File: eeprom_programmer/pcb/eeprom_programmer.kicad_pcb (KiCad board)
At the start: 2 copper layers, 60 x 60 mm, 16 parts, among them M1 MountingHole_3.2mm_M3_Pad, M2 MountingHole_3.2mm_M3_Pad, M3 MountingHole_3.2mm_M3_Pad, M4 MountingHole_3.2mm_M3_Pad, SW1 SW_DIP_x03, U1 74HC595, U2 74HC595, U3 74HC595, U4 SST39SF040, U5 AT28C64B

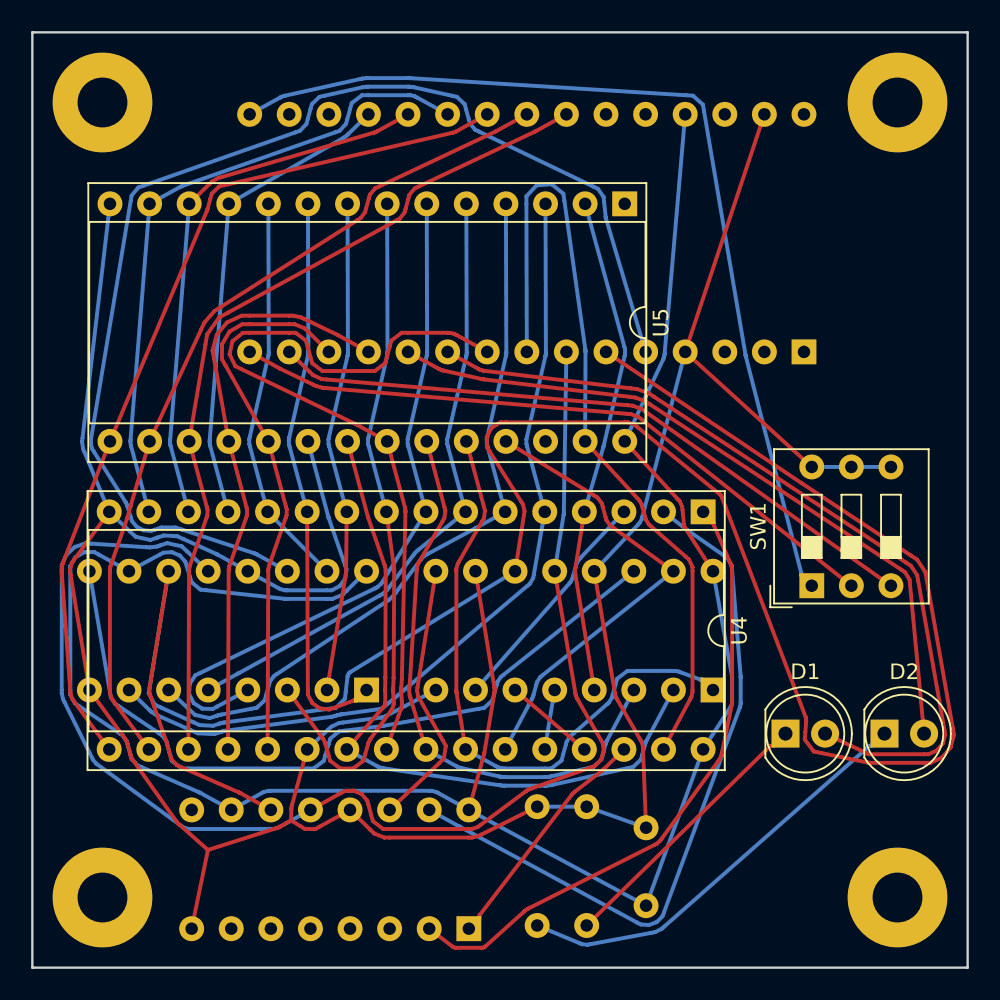
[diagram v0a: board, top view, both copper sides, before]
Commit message: Fix arduino d13 LED pullup bug.
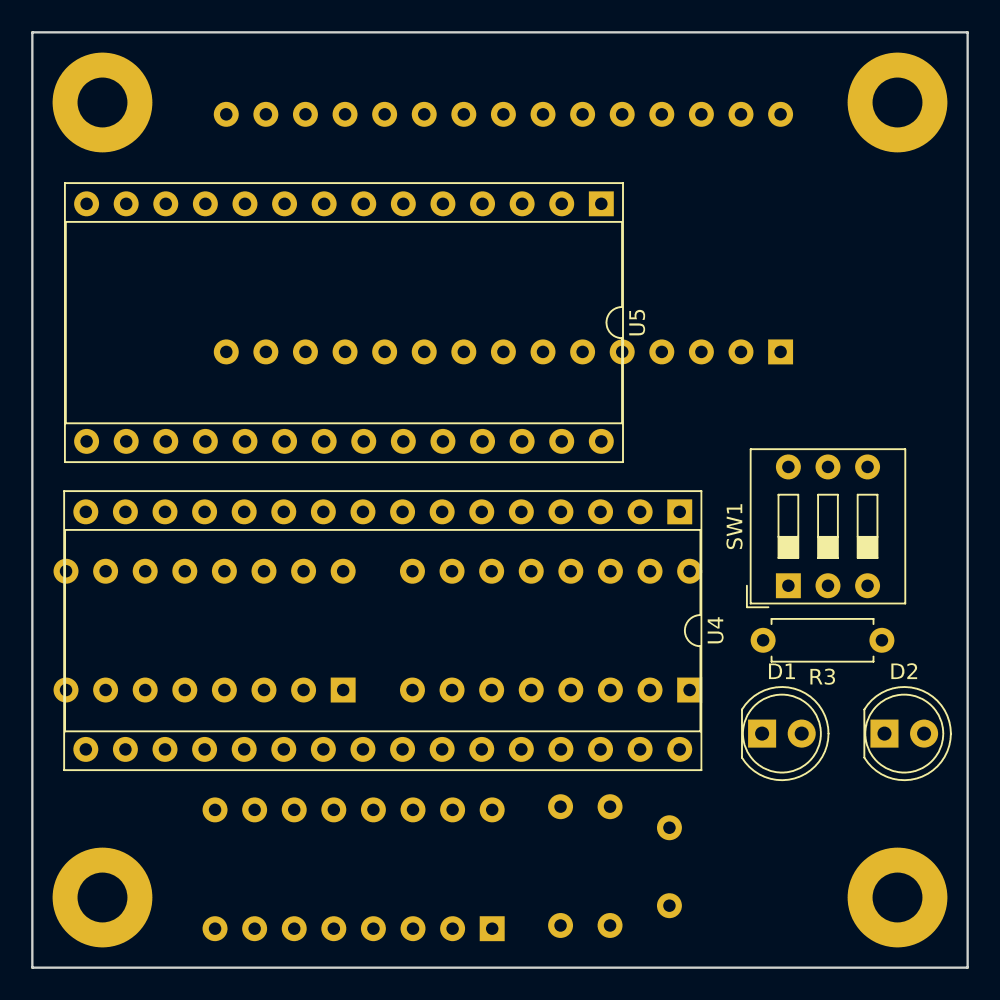
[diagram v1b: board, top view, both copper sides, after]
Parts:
- added R3: 100K, Resistor_THT:R_Axial_DIN0207_L6.3mm_D2.5mm_P7.62mm_Horizontal, F.Cu at (124.5, 59.0)
- moved A1 1.50 mm to (118.0, 40.5)
- moved C1 1.50 mm to (110.9, 76.0)
- moved D1 1.50 mm to (116.8, 65.0)
- moved R1 1.50 mm to (107.1, 77.3)
- moved R2 1.50 mm to (103.9, 77.3)
- moved SW1 1.50 mm to (118.5, 55.5)
- moved U1 1.50 mm to (89.9, 62.2)
- moved U2 1.50 mm to (112.2, 62.2)
- moved U3 1.50 mm to (99.5, 77.5)
- moved U4 1.50 mm to (111.5, 50.8)
- moved U5 1.50 mm to (106.5, 31.0)
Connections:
- SW1 pad 6: GND -> +5V
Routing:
- net GND: track 185.8 -> 0.00 mm
- net /SRCLK: track 145.1 -> 0.00 mm
- net +5V: track 142.5 -> 0.00 mm
- net /RCLK: track 87.8 -> 0.00 mm
- net /SER: track 78.0 -> 0.00 mm
- net Net-(A1-Pad16): track 61.6 -> 0.00 mm
- net /D3: track 56.9 -> 0.00 mm
- net /D5: track 54.7 -> 0.00 mm
- net /A7: track 54.5 -> 0.00 mm
- net /D4: track 54.4 -> 0.00 mm
- net Net-(A1-Pad10): track 53.3 -> 0.00 mm
- net /~OE: track 52.4 -> 0.00 mm
- net /~WE: track 51.8 -> 0.00 mm
- net Net-(U1-Pad9): track 49.1 -> 0.00 mm
- net /A6: track 47.2 -> 0.00 mm
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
